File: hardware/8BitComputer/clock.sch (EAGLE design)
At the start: 11 parts, among them IC1 LM555CN, J1 Power

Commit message: just need to route
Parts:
- added C4, C5, C6: 0.1 uF, passives:C-USC0805
- added J2: Clock Output, connector:M06SILK_FEMALE_PTH
- added LED2: Green, leds:LED-3MM-NO_SILK
- added LED3: White, leds:LED-3MM-NO_SILK
- added Q1, Q2: P2N2222AZL1G, transitors:P2N2222AZL1G
- added R5: 4.7 K, passives:RESISTOR0805-RES
- added R6, R7: 100 R, passives:RESISTOR0805-RES
- added R8, R9: 1 K, passives:RESISTOR0805-RES
- added S1: 555 or Manual, switches:SWITCH-SPSTKIT
- added S2: Halt, switches:SWITCH-SPSTKIT
- added U$2: SWITCH_TACTILETACTILE_PIN, switches:SWITCH_TACTILETACTILE_PIN
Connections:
- new net CLOCK_OUT: C6.2, J2.1, J2.2, J2.3, J2.4, J2.5, J2.6, Q2.E, R7.2
- new net MANUAL_TIMER: C4.1, LED2.A, S1.O, U$2.A
- new net N$10: Q1.E, Q2.C
- new net N$11: R8.2, S2.P
- new net N$12: Q1.B, R9.2
- new net N$5: LED2.C, R6.1
- new net N$6: R5.1, U$2.C
- new net N$7: LED3.C, R7.1
- new net N$8: Q2.B, S2.O
- new net SWITCHED_CLOCK_OUT: C5.2, R9.1, S1.P
- net 555-1-OUT: now also S1.S
- net GND: now also C4.2, C5.1, C6.1, Q1.C, R6.2
- net VCC5V: now also LED3.A, R5.2, R8.1

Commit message: organized board
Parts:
- added J3: (no value), connector:M08SILK_FEMALE_PTH
- added J4, J5: Power, connector:M02PTH
- J2: value Clock Output -> Power; device connector:M06SILK_FEMALE_PTH -> connector:M02PTH
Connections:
- net CLOCK_OUT: now also J3.2, J3.3, J3.4, J3.5, J3.6, J3.7; no longer J2.1, J2.2, J2.3, J2.4, J2.5, J2.6
- net GND: now also J2.2, J3.8, J4.2, J5.2
- net VCC5V: now also J2.1, J3.1, J4.1, J5.1
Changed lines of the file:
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@@
 <part name="R8" library="passives" deviceset="RESISTOR" device="0805-RES" value="1 K"/>
 <part name="R9" library="passives" deviceset="RESISTOR" device="0805-RES" value="1 K"/>
-<part name="J2" library="connector" deviceset="M06" device="SILK_FEMALE_PTH" value="Clock Output"/>
 <part name="C6" library="passives" deviceset="C-US" device="C0805" value="0.1 uF"/>
+<part name="J3" library="connector" deviceset="M08" device="SILK_FEMALE_PTH"/>
+<part name="J2" library="connector" deviceset="M02" device="PTH" value="Power"/>
+<part name="J4" library="connector" deviceset="M02" device="PTH" value="Power"/>
+<part name="J5" library="connector" deviceset="M02" device="PTH" value="Power"/>
 </parts>
 <sheets>
@@
 <attribute name="NAME" x="22.86" y="10.922" size="1.778" layer="95"/>
 </instance>
+<instance part="J2" gate="G$1" x="58.42" y="5.08" smashed="yes">
+<attribute name="VALUE" x="55.88" y="0" size="1.778" layer="96"/>
+<attribute name="NAME" x="55.88" y="10.922" size="1.778" layer="95"/>
+</instance>
+<instance part="J4" gate="G$1" x="91.44" y="5.08" smashed="yes">
+<attribute name="VALUE" x="88.9" y="0" size="1.778" layer="96"/>
+<attribute name="NAME" x="88.9" y="10.922" size="1.778" layer="95"/>
+</instance>
+<instance part="J5" gate="G$1" x="119.38" y="5.08" smashed="yes">
+<attribute name="VALUE" x="116.84" y="0" size="1.778" layer="96"/>
+<attribute name="NAME" x="116.84" y="10.922" size="1.778" layer="95"/>
+</instance>
 </instances>
 <busses>
@@
 <label x="40.64" y="5.08" size="1.778" layer="95"/>
 </segment>
+<segment>
+<pinref part="J2" gate="G$1" pin="1"/>
+<wire x1="66.04" y1="5.08" x2="71.12" y2="5.08" width="0.1524" layer="91"/>
+<label x="73.66" y="5.08" size="1.778" layer="95"/>
+</segment>
+<segment>
+<pinref part="J4" gate="G$1" pin="1"/>
+<wire x1="99.06" y1="5.08" x2="104.14" y2="5.08" width="0.1524" layer="91"/>
+<label x="106.68" y="5.08" size="1.778" layer="95"/>
+</segment>
+<segment>
+<pinref part="J5" gate="G$1" pin="1"/>
+<wire x1="127" y1="5.08" x2="132.08" y2="5.08" width="0.1524" layer="91"/>
+<label x="134.62" y="5.08" size="1.778" layer="95"/>
+</segment>
 </net>
 <net name="GND" class="0">
@@
 <wire x1="33.02" y1="7.62" x2="38.1" y2="7.62" width="0.1524" layer="91"/>
 <label x="38.1" y="7.62" size="1.778" layer="95"/>
+</segment>
+<segment>
+<pinref part="J2" gate="G$1" pin="2"/>
+<wire x1="66.04" y1="7.62" x2="71.12" y2="7.62" width="0.1524" layer="91"/>
+<label x="71.12" y="7.62" size="1.778" layer="95"/>
+</segment>
+<segment>
+<pinref part="J4" gate="G$1" pin="2"/>
+<wire x1="99.06" y1="7.62" x2="104.14" y2="7.62" width="0.1524" layer="91"/>
+<label x="104.14" y="7.62" size="1.778" layer="95"/>
+</segment>
+<segment>
+<pinref part="J5" gate="G$1" pin="2"/>
+<wire x1="127" y1="7.62" x2="132.08" y2="7.62" width="0.1524" layer="91"/>
+<label x="132.08" y="7.62" size="1.778" layer="95"/>
 </segment>
 </net>
@@
 <attribute name="VALUE" x="74.93" y="60.198" size="1.778" layer="96"/>
 </instance>
-<instance part="J2" gate="G$1" x="162.56" y="25.4" smashed="yes" rot="R180">
-<attribute name="VALUE" x="167.64" y="35.56" size="1.778" layer="96" rot="R180"/>
-<attribute name="NAME" x="167.64" y="14.478" size="1.778" layer="95" rot="R180"/>
-</instance>
 <instance part="C6" gate="G$1" x="114.3" y="20.32" smashed="yes" rot="R180">
 <attribute name="NAME" x="118.364" y="17.145" size="1.778" layer="95" rot="R180"/>
 <attribute name="VALUE" x="113.284" y="24.511" size="1.778" layer="96" rot="R180"/>
+</instance>
+<instance part="J3" gate="G$1" x="165.1" y="25.4" smashed="yes" rot="R180">
+<attribute name="VALUE" x="170.18" y="38.1" size="1.778" layer="96" rot="R180"/>
+<attribute name="NAME" x="170.18" y="11.938" size="1.778" layer="95" rot="R180"/>
 </instance>
 </instances>
@@
 <label x="114.3" y="7.62" size="1.778" layer="95"/>
 </segment>
+<segment>
+<pinref part="J3" gate="G$1" pin="8"/>
+<wire x1="160.02" y1="15.24" x2="160.02" y2="12.7" width="0.1524" layer="91"/>
+<label x="157.48" y="10.16" size="1.778" layer="95"/>
+</segment>
 </net>
 <net name="N$11" class="0">
@@
 <wire x1="81.28" y1="25.4" x2="76.2" y2="25.4" width="0.1524" layer="91"/>
 <label x="71.12" y="25.4" size="1.778" layer="95"/>
+</segment>
+<segment>
+<pinref part="J3" gate="G$1" pin="1"/>
+<wire x1="160.02" y1="33.02" x2="160.02" y2="35.56" width="0.1524" layer="91"/>
+<label x="157.48" y="35.56" size="1.778" layer="95"/>
 </segment>
 </net>
@@
 <pinref part="R7" gate="G$1" pin="2"/>
 <junction x="101.6" y="25.4"/>
-<pinref part="J2" gate="G$1" pin="3"/>
 <wire x1="101.6" y1="25.4" x2="114.3" y2="25.4" width="0.1524" layer="91"/>
-<pinref part="J2" gate="G$1" pin="2"/>
 <wire x1="114.3" y1="25.4" x2="157.48" y2="25.4" width="0.1524" layer="91"/>
+<junction x="157.48" y="25.4"/>
 <wire x1="157.48" y1="25.4" x2="157.48" y2="27.94" width="0.1524" layer="91"/>
-<junction x="157.48" y="25.4"/>
-<pinref part="J2" gate="G$1" pin="1"/>
 <wire x1="157.48" y1="27.94" x2="157.48" y2="30.48" width="0.1524" layer="91"/>
-<junction x="157.48" y="27.94"/>
-<pinref part="J2" gate="G$1" pin="4"/>
 <wire x1="157.48" y1="25.4" x2="157.48" y2="22.86" width="0.1524" layer="91"/>
-<pinref part="J2" gate="G$1" pin="5"/>
-<wire x1="157.48" y1="22.86" x2="157.48" y2="20.32" width="0.1524" layer="91"/>
-<junction x="157.48" y="22.86"/>
-<pinref part="J2" gate="G$1" pin="6"/>
-<wire x1="157.48" y1="20.32" x2="157.48" y2="17.78" width="0.1524" layer="91"/>
-<junction x="157.48" y="20.32"/>
 <pinref part="C6" gate="G$1" pin="2"/>
 <junction x="114.3" y="25.4"/>
-</segment>
-</net>
+<pinref part="J3" gate="G$1" pin="4"/>
+<wire x1="157.48" y1="22.86" x2="157.48" y2="20.32" width="0.1524" layer="91"/>
+<wire x1="157.48" y1="20.32" x2="157.48" y2="17.78" width="0.1524" layer="91"/>
+<wire x1="157.48" y1="25.4" x2="160.02" y2="25.4" width="0.1524" layer="91"/>
+<pinref part="J3" gate="G$1" pin="3"/>
+<wire x1="160.02" y1="27.94" x2="157.48" y2="27.94" width="0.1524" layer="91"/>
+<junction x="157.48" y="27.94"/>
+<pinref part="J3" gate="G$1" pin="2"/>
+<wire x1="160.02" y1="30.48" x2="157.48" y2="30.48" width="0.1524" layer="91"/>
+<pinref part="J3" gate="G$1" pin="5"/>
+<wire x1="160.02" y1="22.86" x2="157.48" y2="22.86" width="0.1524" layer="91"/>
+<junction x="157.48" y="22.86"/>
+<pinref part="J3" gate="G$1" pin="6"/>
+<wire x1="160.02" y1="20.32" x2="157.48" y2="20.32" width="0.1524" layer="91"/>
+<junction x="157.48" y="20.32"/>
+<pinref part="J3" gate="G$1" pin="7"/>
+<wire x1="160.02" y1="17.78" x2="157.48" y2="17.78" width="0.1524" layer="91"/>
+</segment>
+</net>

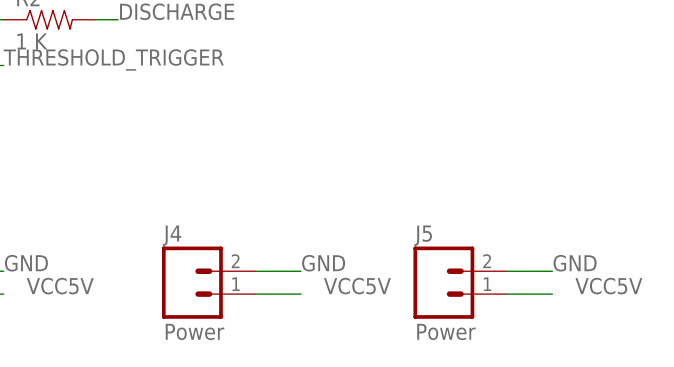
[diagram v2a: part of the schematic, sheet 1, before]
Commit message: Sons first Routed Board
Using ground plane on 2nd side of board to make layout easier.
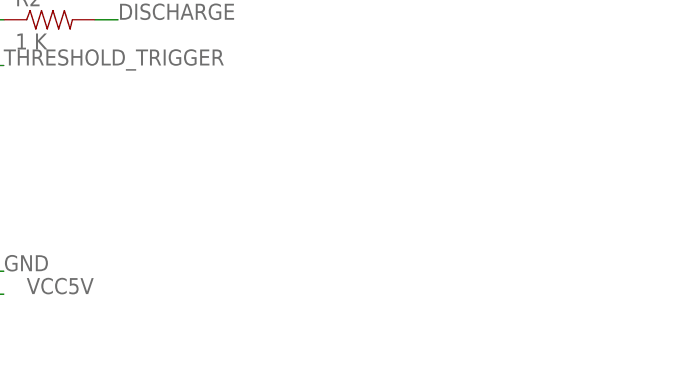
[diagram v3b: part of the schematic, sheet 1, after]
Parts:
- removed J4, J5: Power, connector:M02PTH
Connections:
- net GND: no longer J4.2, J5.2
- net VCC5V: no longer J4.1, J5.1
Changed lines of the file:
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@@
 <drawing>
 <settings>
-<setting alwaysvectorfont="yes"/>
+<setting alwaysvectorfont="no"/>
 <setting verticaltext="up"/>
 </settings>
@@
 <part name="J3" library="connector" deviceset="M08" device="SILK_FEMALE_PTH"/>
 <part name="J2" library="connector" deviceset="M02" device="PTH" value="Power"/>
-<part name="J4" library="connector" deviceset="M02" device="PTH" value="Power"/>
-<part name="J5" library="connector" deviceset="M02" device="PTH" value="Power"/>
 </parts>
 <sheets>
@@
 <attribute name="NAME" x="55.88" y="10.922" size="1.778" layer="95"/>
 </instance>
-<instance part="J4" gate="G$1" x="91.44" y="5.08" smashed="yes">
-<attribute name="VALUE" x="88.9" y="0" size="1.778" layer="96"/>
-<attribute name="NAME" x="88.9" y="10.922" size="1.778" layer="95"/>
-</instance>
-<instance part="J5" gate="G$1" x="119.38" y="5.08" smashed="yes">
-<attribute name="VALUE" x="116.84" y="0" size="1.778" layer="96"/>
-<attribute name="NAME" x="116.84" y="10.922" size="1.778" layer="95"/>
-</instance>
 </instances>
 <busses>
@@
 <label x="73.66" y="5.08" size="1.778" layer="95"/>
 </segment>
-<segment>
-<pinref part="J4" gate="G$1" pin="1"/>
-<wire x1="99.06" y1="5.08" x2="104.14" y2="5.08" width="0.1524" layer="91"/>
-<label x="106.68" y="5.08" size="1.778" layer="95"/>
-</segment>
-<segment>
-<pinref part="J5" gate="G$1" pin="1"/>
-<wire x1="127" y1="5.08" x2="132.08" y2="5.08" width="0.1524" layer="91"/>
-<label x="134.62" y="5.08" size="1.778" layer="95"/>
-</segment>
 </net>
 <net name="GND" class="0">
@@
 <label x="71.12" y="7.62" size="1.778" layer="95"/>
 </segment>
-<segment>
-<pinref part="J4" gate="G$1" pin="2"/>
-<wire x1="99.06" y1="7.62" x2="104.14" y2="7.62" width="0.1524" layer="91"/>
-<label x="104.14" y="7.62" size="1.778" layer="95"/>
-</segment>
-<segment>
-<pinref part="J5" gate="G$1" pin="2"/>
-<wire x1="127" y1="7.62" x2="132.08" y2="7.62" width="0.1524" layer="91"/>
-<label x="132.08" y="7.62" size="1.778" layer="95"/>
-</segment>
 </net>

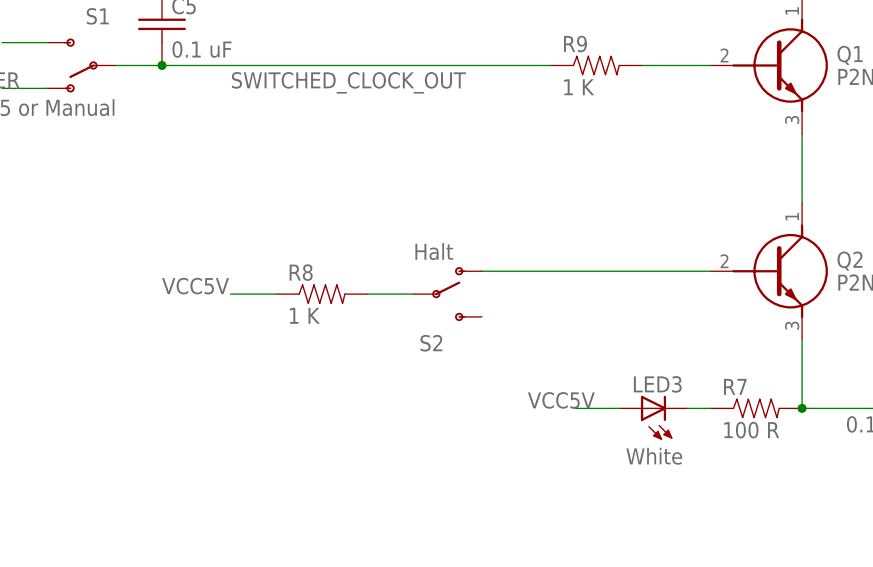
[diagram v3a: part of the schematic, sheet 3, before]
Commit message: thicked traces: moved the resitor on halt switch so it can be pull up or pull down
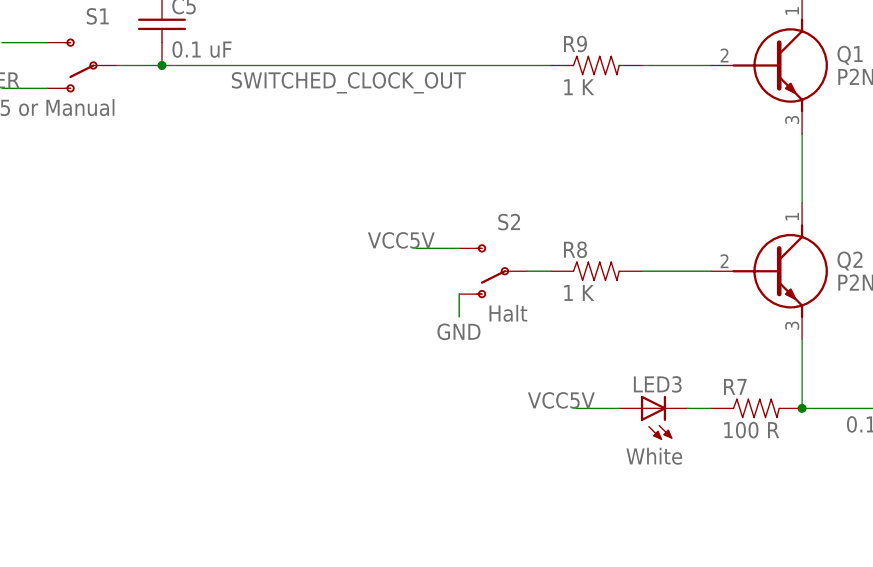
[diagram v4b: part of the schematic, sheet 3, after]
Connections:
- removed net N$11: R8.2, S2.P
- new net N$9: Q2.B, R8.2
- net GND: now also S2.O
- net N$8: now also R8.1, S2.P; no longer Q2.B, S2.O
- net VCC5V: now also S2.S; no longer R8.1
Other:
- moved on the sheet: R8, S2
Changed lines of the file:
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@@
 <drawing>
 <settings>
-<setting alwaysvectorfont="no"/>
+<setting alwaysvectorfont="yes"/>
 <setting verticaltext="up"/>
 </settings>
@@
 <attribute name="VALUE" x="105.41" y="39.37" size="1.778" layer="96" align="center-left"/>
 </instance>
-<instance part="S2" gate="1" x="60.96" y="38.1" smashed="yes">
-<attribute name="NAME" x="59.055" y="31.75" size="1.778" layer="95"/>
-<attribute name="VALUE" x="58.42" y="41.91" size="1.778" layer="96"/>
-</instance>
-<instance part="R8" gate="G$1" x="48.26" y="38.1" smashed="yes">
-<attribute name="NAME" x="44.45" y="39.5986" size="1.778" layer="95"/>
-<attribute name="VALUE" x="44.45" y="34.798" size="1.778" layer="96"/>
+<instance part="S2" gate="1" x="68.58" y="40.64" smashed="yes" rot="R180">
+<attribute name="NAME" x="70.485" y="46.99" size="1.778" layer="95" rot="R180"/>
+<attribute name="VALUE" x="71.12" y="36.83" size="1.778" layer="96" rot="R180"/>
+</instance>
+<instance part="R8" gate="G$1" x="78.74" y="40.64" smashed="yes">
+<attribute name="NAME" x="74.93" y="42.1386" size="1.778" layer="95"/>
+<attribute name="VALUE" x="74.93" y="37.338" size="1.778" layer="96"/>
 </instance>
 <instance part="R9" gate="G$1" x="78.74" y="63.5" smashed="yes">
@@
 <label x="157.48" y="10.16" size="1.778" layer="95"/>
 </segment>
-</net>
-<net name="N$11" class="0">
-<segment>
-<pinref part="R8" gate="G$1" pin="2"/>
-<pinref part="S2" gate="1" pin="P"/>
-<wire x1="53.34" y1="38.1" x2="58.42" y2="38.1" width="0.1524" layer="91"/>
+<segment>
+<pinref part="S2" gate="1" pin="O"/>
+<wire x1="63.5" y1="38.1" x2="63.5" y2="35.56" width="0.1524" layer="91"/>
+<label x="60.96" y="33.02" size="1.778" layer="95"/>
 </segment>
 </net>
 <net name="VCC5V" class="0">
-<segment>
-<pinref part="R8" gate="G$1" pin="1"/>
-<wire x1="43.18" y1="38.1" x2="38.1" y2="38.1" width="0.1524" layer="91"/>
-<label x="30.48" y="38.1" size="1.778" layer="95"/>
-</segment>
 <segment>
 <pinref part="LED3" gate="G$1" pin="A"/>
@@
 <label x="157.48" y="35.56" size="1.778" layer="95"/>
 </segment>
-</net>
-<net name="N$8" class="0">
-<segment>
-<pinref part="S2" gate="1" pin="O"/>
-<pinref part="Q2" gate="G$1" pin="B"/>
-<wire x1="66.04" y1="40.64" x2="91.44" y2="40.64" width="0.1524" layer="91"/>
+<segment>
+<pinref part="S2" gate="1" pin="S"/>
+<wire x1="63.5" y1="43.18" x2="58.42" y2="43.18" width="0.1524" layer="91"/>
+<label x="53.34" y="43.18" size="1.778" layer="95"/>
 </segment>
 </net>
@@
 </segment>
 </net>
+<net name="N$8" class="0">
+<segment>
+<pinref part="S2" gate="1" pin="P"/>
+<pinref part="R8" gate="G$1" pin="1"/>
+<wire x1="71.12" y1="40.64" x2="73.66" y2="40.64" width="0.1524" layer="91"/>
+</segment>
+</net>
+<net name="N$9" class="0">
+<segment>
+<pinref part="R8" gate="G$1" pin="2"/>
+<pinref part="Q2" gate="G$1" pin="B"/>
+<wire x1="83.82" y1="40.64" x2="91.44" y2="40.64" width="0.1524" layer="91"/>
+</segment>
+</net>
